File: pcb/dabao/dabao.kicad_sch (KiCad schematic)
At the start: 68 parts, among them J1 Conn_01x05, J2 USB_C_Receptacle_USB2.0_16P, J3 Conn_01x04, J4 MagConn_01x04_Pin, J5 Conn_Battery, J6 Conn_01x04, J7 Conn_01x04, J8 Display, SW1 SW_RESET, SW2 SW_POWER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

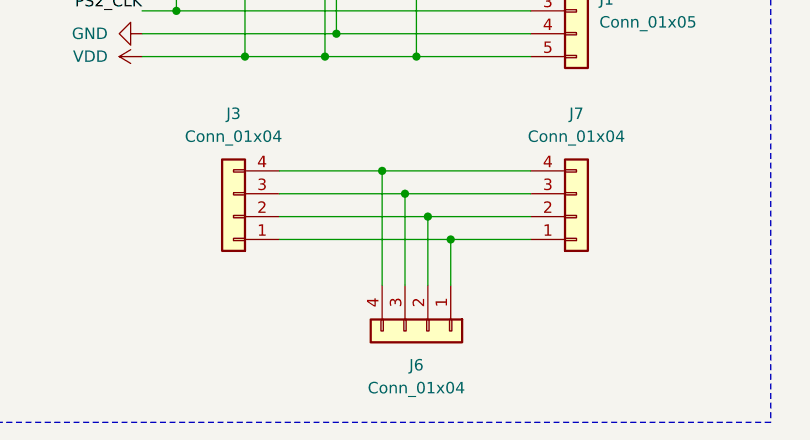
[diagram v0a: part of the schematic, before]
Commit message: Revert "Update outline for mounting holes"
This reverts commit 8c40ebd10364a523e89f308933ebed6ba8cc3b75.
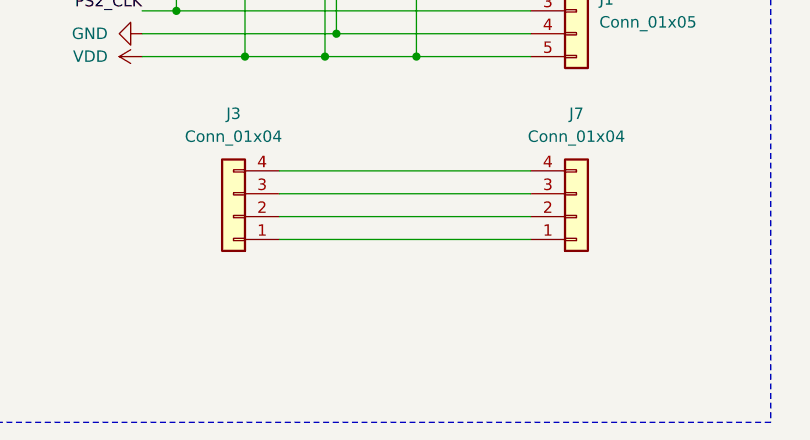
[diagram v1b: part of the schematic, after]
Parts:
- removed J6: Conn_01x04, Library:TPSensorModule_Connector, symbol Connector_Generic:Conn_01x04
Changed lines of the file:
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@@
 	)
 	(junction
-		(at 67.31 170.18)
-		(diameter 0)
-		(color 0 0 0 0)
-	)
-	(junction
 		(at 54.61 39.37)
 		(diameter 0)
@@
 	)
 	(junction
-		(at 64.77 167.64)
-		(diameter 0)
-		(color 0 0 0 0)
-	)
-	(junction
 		(at 46.99 152.4)
 		(diameter 0)
@@
 	)
 	(junction
-		(at 69.85 172.72)
-		(diameter 0)
-		(color 0 0 0 0)
-	)
-	(junction
 		(at 44.45 55.88)
 		(diameter 0)
@@
 	)
 	(junction
-		(at 62.23 165.1)
-		(diameter 0)
-		(color 0 0 0 0)
-	)
-	(junction
 		(at 59.69 52.07)
 		(diameter 0)
@@
 	(wire
 		(pts
-			(xy 50.8 172.72) (xy 69.85 172.72)
+			(xy 50.8 172.72) (xy 78.74 172.72)
 		)
 		(stroke
@@
 	(wire
 		(pts
-			(xy 67.31 170.18) (xy 78.74 170.18)
-		)
-		(stroke
-			(width 0)
-			(type default)
-		)
-	)
-	(wire
-		(pts
 			(xy 49.53 52.07) (xy 59.69 52.07)
 		)
@@
 	(wire
 		(pts
-			(xy 62.23 177.8) (xy 62.23 165.1)
-		)
-		(stroke
-			(width 0)
-			(type default)
-		)
-	)
-	(wire
-		(pts
-			(xy 50.8 165.1) (xy 62.23 165.1)
+			(xy 50.8 165.1) (xy 78.74 165.1)
 		)
 		(stroke
@@
 	(wire
 		(pts
-			(xy 64.77 167.64) (xy 64.77 177.8)
-		)
-		(stroke
-			(width 0)
-			(type default)
-		)
-	)
-	(wire
-		(pts
 			(xy 175.26 29.21) (xy 175.26 31.75)
 		)
@@
 	(wire
 		(pts
-			(xy 50.8 167.64) (xy 64.77 167.64)
+			(xy 50.8 167.64) (xy 78.74 167.64)
 		)
 		(stroke
@@
 	(wire
 		(pts
-			(xy 64.77 167.64) (xy 78.74 167.64)
-		)
-		(stroke
-			(width 0)
-			(type default)
-		)
-	)
-	(wire
-		(pts
 			(xy 80.01 101.6) (xy 90.17 101.6)
 		)
@@
 	(wire
 		(pts
-			(xy 50.8 170.18) (xy 67.31 170.18)
+			(xy 50.8 170.18) (xy 78.74 170.18)
 		)
 		(stroke
@@
 	(wire
 		(pts
-			(xy 62.23 165.1) (xy 78.74 165.1)
-		)
-		(stroke
-			(width 0)
-			(type default)
-		)
-	)
-	(wire
-		(pts
 			(xy 64.77 39.37) (xy 64.77 55.88)
 		)
@@
 	(wire
 		(pts
-			(xy 67.31 177.8) (xy 67.31 170.18)
-		)
-		(stroke
-			(width 0)
-			(type default)
-		)
-	)
-	(wire
-		(pts
 			(xy 69.85 52.07) (xy 80.01 52.07)
 		)
@@
 	(wire
 		(pts
-			(xy 69.85 172.72) (xy 69.85 177.8)
-		)
-		(stroke
-			(width 0)
-			(type default)
-		)
-	)
-	(wire
-		(pts
 			(xy 64.77 135.89) (xy 64.77 144.78)
 		)
@@
 	(wire
 		(pts
-			(xy 69.85 172.72) (xy 78.74 172.72)
-		)
-		(stroke
-			(width 0)
-			(type default)
-		)
-	)
-	(wire
-		(pts
 			(xy 184.15 76.2) (xy 189.23 76.2)
 		)
@@
 					(unit 1)
 				)
-			)
-		)
-	)
-	(symbol
-		(lib_id "Connector_Generic:Conn_01x04")
-		(at 67.31 182.88 270)
-		(unit 1)
-		(exclude_from_sim no)
-		(in_bom yes)
-		(on_board yes)
-		(dnp no)
-		(fields_autoplaced yes)
-		(property "Reference" "J6"
-			(at 66.04 186.69 90)
-			(effects
-				(font
-					(size 1.27 1.27)
-				)
-			)
-		)
-		(property "Value" "Conn_01x04"
-			(at 66.04 189.23 90)
-			(effects
-				(font
-					(size 1.27 1.27)
-				)
-			)
-		)
-		(property "Footprint" "Library:TPSensorModule_Connector"
-			(at 67.31 182.88 0)
-			(effects
-				(font
-					(size 1.27 1.27)
-				)
-				(hide yes)
-			)
-		)
-		(property "Datasheet" "~"
-			(at 67.31 182.88 0)
-			(effects
-				(font
-					(size 1.27 1.27)
-				)
-				(hide yes)
-			)
-		)
-		(property "Description" "Generic connector, single row, 01x04, script generated (kicad-library-utils/schlib/autogen/connector/)"
-			(at 67.31 182.88 0)
-			(effects
-				(font
-					(size 1.27 1.27)
-				)
-				(hide yes)
-			)
-		)
-		(pin "4"
-		)
-		(pin "1"
-		)
-		(pin "3"
-		)
-		(pin "2"
-		)
-		(instances
-			(project "dabao"
-				(path "/f7dfc45c-83ad-43c7-9815-463af0b28fbd"
-					(reference "J6")
-					(unit 1)
-				)

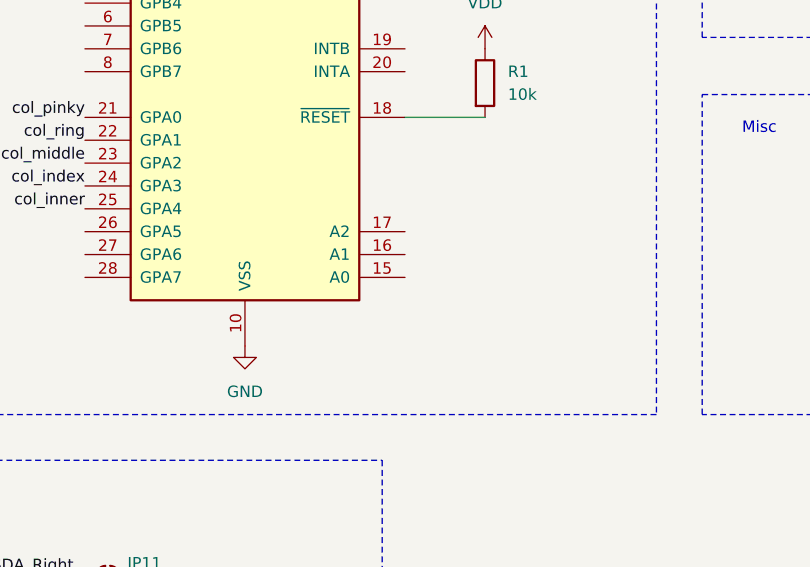
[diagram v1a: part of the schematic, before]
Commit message: PCB updates to fix assembly issues
Addresses https://github.com/justinmklam/dabao/issues/1
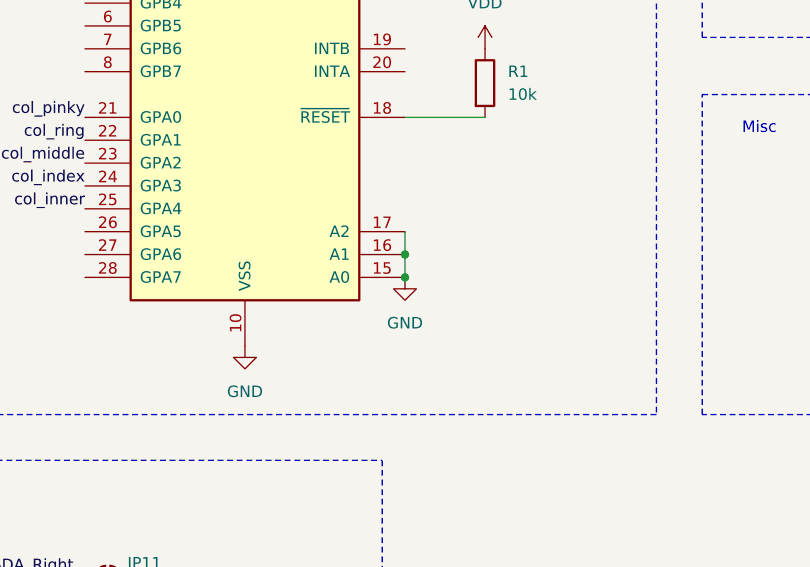
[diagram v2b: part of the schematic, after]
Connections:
- net GND: now also U2.15 (A0), U2.16 (A1), U2.17 (A2)
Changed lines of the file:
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@@
 	)
 	(junction
+		(at 175.26 132.08)
+		(diameter 0)
+		(color 0 0 0 0)
+	)
+	(junction
 		(at 85.09 55.88)
 		(diameter 0)
@@
 	)
 	(junction
+		(at 175.26 129.54)
+		(diameter 0)
+		(color 0 0 0 0)
+	)
+	(junction
 		(at 57.15 149.86)
 		(diameter 0)
@@
 	(wire
 		(pts
+			(xy 175.26 129.54) (xy 175.26 132.08)
+		)
+		(stroke
+			(width 0)
+			(type default)
+		)
+	)
+	(wire
+		(pts
 			(xy 50.8 165.1) (xy 78.74 165.1)
 		)
@@
 	(wire
 		(pts
+			(xy 175.26 127) (xy 175.26 129.54)
+		)
+		(stroke
+			(width 0)
+			(type default)
+		)
+	)
+	(wire
+		(pts
 			(xy 236.22 44.45) (xy 242.57 44.45)
 		)
@@
 		)
 		(instances
-			(project "dabao-choc"
+			(project "dabao"
 				(path "/f7dfc45c-83ad-43c7-9815-463af0b28fbd"
 					(reference "D5")
@@
 		)
 		(instances
-			(project "dabao-choc"
+			(project "dabao"
 				(path "/f7dfc45c-83ad-43c7-9815-463af0b28fbd"
 					(reference "D12")
@@
 		)
 		(instances
-			(project "dabao-choc"
+			(project "dabao"
 				(path "/f7dfc45c-83ad-43c7-9815-463af0b28fbd"
 					(reference "S16")
@@
 		)
 		(instances
-			(project "dabao-choc"
+			(project "dabao"
 				(path "/f7dfc45c-83ad-43c7-9815-463af0b28fbd"
 					(reference "S3")
@@
 		)
 		(instances
-			(project ""
+			(project "dabao"
 				(path "/f7dfc45c-83ad-43c7-9815-463af0b28fbd"
 					(reference "U2")
@@
 		)
 		(instances
-			(project "dabao-choc"
+			(project "dabao"
 				(path "/f7dfc45c-83ad-43c7-9815-463af0b28fbd"
 					(reference "D16")
@@
 		)
 		(instances
-			(project ""
+			(project "dabao"
 				(path "/f7dfc45c-83ad-43c7-9815-463af0b28fbd"
 					(reference "JP13")
@@
 		)
 		(instances
-			(project "dabao-choc"
+			(project "dabao"
 				(path "/f7dfc45c-83ad-43c7-9815-463af0b28fbd"
 					(reference "D15")
@@
 		)
 		(instances
-			(project ""
+			(project "dabao"
 				(path "/f7dfc45c-83ad-43c7-9815-463af0b28fbd"
 					(reference "U1")
@@
 		)
 		(instances
-			(project "dabao-choc"
+			(project "dabao"
 				(path "/f7dfc45c-83ad-43c7-9815-463af0b28fbd"
 					(reference "D11")
@@
 		)
 		(instances
-			(project "dabao-choc"
+			(project "dabao"
 				(path "/f7dfc45c-83ad-43c7-9815-463af0b28fbd"
 					(reference "D17")
@@
 		)
 		(instances
-			(project "dabao-choc"
+			(project "dabao"
 				(path "/f7dfc45c-83ad-43c7-9815-463af0b28fbd"
 					(reference "D4")
@@
 		)
 		(instances
-			(project ""
+			(project "dabao"
 				(path "/f7dfc45c-83ad-43c7-9815-463af0b28fbd"
 					(reference "JP1")
@@
 		)
 		(instances
-			(project "dabao-choc"
+			(project "dabao"
 				(path "/f7dfc45c-83ad-43c7-9815-463af0b28fbd"
 					(reference "D9")
@@
 		)
 		(instances
-			(project ""
+			(project "dabao"
 				(path "/f7dfc45c-83ad-43c7-9815-463af0b28fbd"
 					(reference "R1")
@@
 		)
 		(instances
-			(project "dabao-choc"
+			(project "dabao"
 				(path "/f7dfc45c-83ad-43c7-9815-463af0b28fbd"
 					(reference "S2")
@@
 		)
 		(instances
-			(project "dabao-choc"
+			(project "dabao"
 				(path "/f7dfc45c-83ad-43c7-9815-463af0b28fbd"
 					(reference "D10")
@@
 		)
 		(instances
-			(project "dabao-choc"
+			(project "dabao"
 				(path "/f7dfc45c-83ad-43c7-9815-463af0b28fbd"
 					(reference "S9")
@@
 		)
 		(instances
-			(project "dabao-choc"
+			(project "dabao"
 				(path "/f7dfc45c-83ad-43c7-9815-463af0b28fbd"
 					(reference "D18")
@@
 	)
 	(symbol
+		(lib_id "power:GND")
+		(at 175.26 132.08 0)
+		(unit 1)
+		(exclude_from_sim no)
+		(in_bom yes)
+		(on_board yes)
+		(dnp no)
+		(fields_autoplaced yes)
+		(property "Reference" "#PWR019"
+			(at 175.26 138.43 0)
+			(effects
+				(font
+					(size 1.27 1.27)
+				)
+				(hide yes)
+			)
+		)
+		(property "Value" "GND"
+			(at 175.26 137.16 0)
+			(effects
+				(font
+					(size 1.27 1.27)
+				)
+			)
+		)
+		(property "Footprint" ""
+			(at 175.26 132.08 0)
+			(effects
+				(font
+					(size 1.27 1.27)
+				)
+				(hide yes)
+			)
+		)
+		(property "Datasheet" ""
+			(at 175.26 132.08 0)
+			(effects
+				(font
+					(size 1.27 1.27)
+				)
+				(hide yes)
+			)
+		)
+		(property "Description" "Power symbol creates a global label with name \"GND\" , ground"
+			(at 175.26 132.08 0)
+			(effects
+				(font
+					(size 1.27 1.27)
+				)
+				(hide yes)
+			)
+		)
+		(pin "1"
+		)
+		(instances
+			(project "dabao"
+				(path "/f7dfc45c-83ad-43c7-9815-463af0b28fbd"
+					(reference "#PWR019")
+					(unit 1)
+				)
+			)
+		)
+	)
+	(symbol
 		(lib_id "PCM_marbastlib-choc:choc_v1_SW_HS_CPG135001S30")
 		(at 87.63 91.44 0)
@@
 		)
 		(instances
-			(project "dabao-choc"
+			(project "dabao"
 				(path "/f7dfc45c-83ad-43c7-9815-463af0b28fbd"
 					(reference "S18")
@@
 		)
 		(instances
-			(project "dabao-choc"
+			(project "dabao"
 				(path "/f7dfc45c-83ad-43c7-9815-463af0b28fbd"
 					(reference "J2")
@@
 		)
 		(instances
-			(project "dabao-choc"
+			(project "dabao"
 				(path "/f7dfc45c-83ad-43c7-9815-463af0b28fbd"
 					(reference "S4")
@@
 		)
 		(instances
-			(project ""
+			(project "dabao"
 				(path "/f7dfc45c-83ad-43c7-9815-463af0b28fbd"
 					(reference "J3")
@@
 		)
 		(instances
-			(project "dabao-choc"
+			(project "dabao"
 				(path "/f7dfc45c-83ad-43c7-9815-463af0b28fbd"
 					(reference "S11")
@@
 		)
 		(instances
-			(project ""
+			(project "dabao"
 				(path "/f7dfc45c-83ad-43c7-9815-463af0b28fbd"
 					(reference "#PWR04")
@@
 		)
 		(instances
-			(project "dabao-choc"
+			(project "dabao"
 				(path "/f7dfc45c-83ad-43c7-9815-463af0b28fbd"
 					(reference "S10")
@@
 		)
 		(instances
-			(project "dabao-choc"
+			(project "dabao"
 				(path "/f7dfc45c-83ad-43c7-9815-463af0b28fbd"
 					(reference "S6")
@@
 		)
 		(instances
-			(project "dabao-choc"
+			(project "dabao"
 				(path "/f7dfc45c-83ad-43c7-9815-463af0b28fbd"
 					(reference "S7")
@@
 		)
 		(instances
-			(project "dabao-choc"
+			(project "dabao"
 				(path "/f7dfc45c-83ad-43c7-9815-463af0b28fbd"
 					(reference "D2")
@@
 		)
 		(instances
-			(project "dabao-choc"
+			(project "dabao"
 				(path "/f7dfc45c-83ad-43c7-9815-463af0b28fbd"
 					(reference "S17")
@@
 		)
 		(instances
-			(project ""
+			(project "dabao"
 				(path "/f7dfc45c-83ad-43c7-9815-463af0b28fbd"
 					(reference "J8")
@@
 		)
 		(instances
-			(project "dabao-choc"
+			(project "dabao"
 				(path "/f7dfc45c-83ad-43c7-9815-463af0b28fbd"
 					(reference "S8")
@@
 		)
 		(instances
-			(project "dabao-choc"
+			(project "dabao"
 				(path "/f7dfc45c-83ad-43c7-9815-463af0b28fbd"
 					(reference "S15")
@@
 		)
 		(instances
-			(project "dabao-choc"
+			(project "dabao"
 				(path "/f7dfc45c-83ad-43c7-9815-463af0b28fbd"
 					(reference "S13")
@@
 		)
 		(instances
-			(project ""
+			(project "dabao"
 				(path "/f7dfc45c-83ad-43c7-9815-463af0b28fbd"
 					(reference "D1")
@@
 		)
 		(instances
-			(project "dabao-choc"
+			(project "dabao"
 				(path "/f7dfc45c-83ad-43c7-9815-463af0b28fbd"
 					(reference "D13")
@@
 		)
 		(instances
-			(project "dabao-choc"
+			(project "dabao"
 				(path "/f7dfc45c-83ad-43c7-9815-463af0b28fbd"
 					(reference "S5")
@@
 		)
 		(instances
-			(project "dabao-choc"
+			(project "dabao"
 				(path "/f7dfc45c-83ad-43c7-9815-463af0b28fbd"
 					(reference "S12")
@@
 		)
 		(instances
-			(project "dabao-choc"
+			(project "dabao"
 				(path "/f7dfc45c-83ad-43c7-9815-463af0b28fbd"
 					(reference "D14")
@@
 		)
 		(instances
-			(project "dabao-choc"
+			(project "dabao"
 				(path "/f7dfc45c-83ad-43c7-9815-463af0b28fbd"
 					(reference "D7")
@@
 		)
 		(instances
-			(project ""
+			(project "dabao"
 				(path "/f7dfc45c-83ad-43c7-9815-463af0b28fbd"
 					(reference "J1")
@@
 		)
 		(instances
-			(project "dabao-choc"
+			(project "dabao"
 				(path "/f7dfc45c-83ad-43c7-9815-463af0b28fbd"
 					(reference "S14")
@@
 		)
 		(instances
-			(project ""
+			(project "dabao"
 				(path "/f7dfc45c-83ad-43c7-9815-463af0b28fbd"
 					(reference "C1")
@@
 		)
 		(instances
-			(project ""
+			(project "dabao"
 				(path "/f7dfc45c-83ad-43c7-9815-463af0b28fbd"
 					(reference "S1")
@@
 		)
 		(instances
-			(project "dabao-choc"
+			(project "dabao"
 				(path "/f7dfc45c-83ad-43c7-9815-463af0b28fbd"
 					(reference "D8")
@@
 		)
 		(instances
-			(project "dabao-choc"
+			(project "dabao"
 				(path "/f7dfc45c-83ad-43c7-9815-463af0b28fbd"
 					(reference "D6")
@@
 		)
 		(instances
-			(project "dabao-choc"
+			(project "dabao"
 				(path "/f7dfc45c-83ad-43c7-9815-463af0b28fbd"
 					(reference "D3")
